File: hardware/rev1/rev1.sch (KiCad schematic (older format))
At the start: 28 parts, among them U1 BNO055, U2 MPL3115A2, U3 Teensy3.6, Y1 Crystal_32kHz768

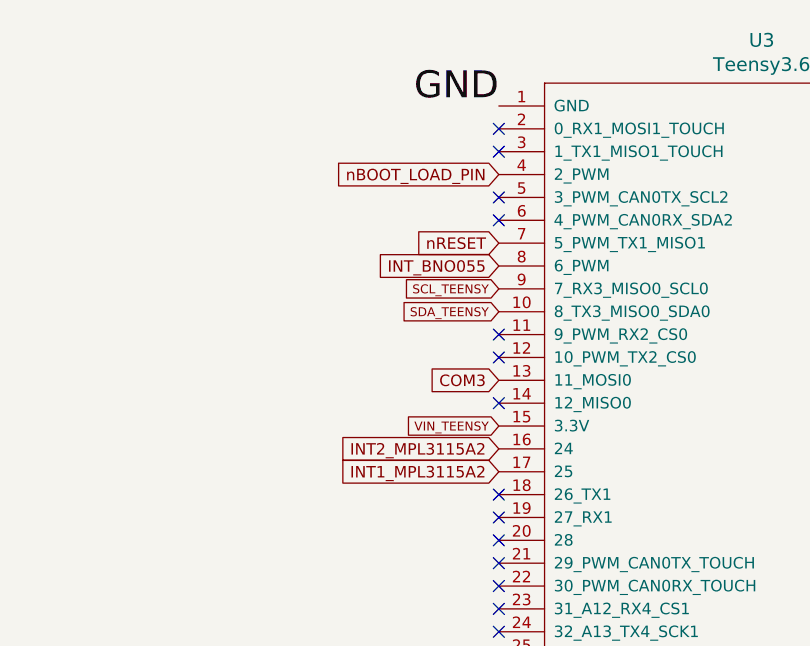
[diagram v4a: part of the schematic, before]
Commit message: mirror all components by flipping and manually reversing sides. Fixes BNO055 and MPL3115 footprint mirroring. (All other components also reversed but symmetrical. Teensy not flipped.) Reassign pins on Teensy.
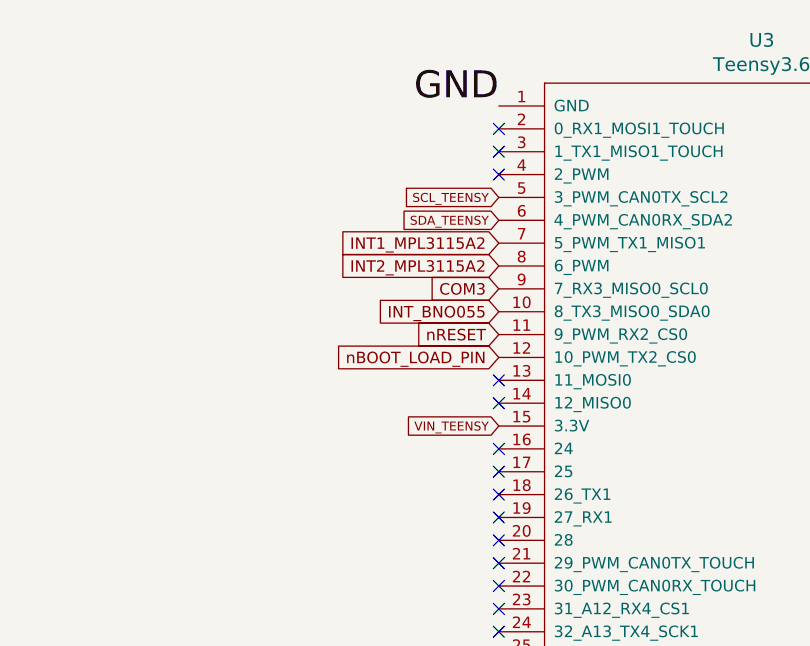
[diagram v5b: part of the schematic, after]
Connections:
- net COM3: now also U3.9 (7_RX3_MISO0_SCL0); no longer U3.13 (11_MOSI0)
- net INT1_MPL3115A2: now also U3.7 (5_PWM_TX1_MISO1); no longer U3.17 (25)
- net INT2_MPL3115A2: now also U3.8 (6_PWM); no longer U3.16 (24)
- net INT_BNO055: now also U3.10 (8_TX3_MISO0_SDA0); no longer U3.8 (6_PWM)
- net SCL_TEENSY: now also U3.5 (3_PWM_CAN0TX_SCL2); no longer U3.9 (7_RX3_MISO0_SCL0)
- net SDA_TEENSY: now also U3.6 (4_PWM_CAN0RX_SDA2); no longer U3.10 (8_TX3_MISO0_SDA0)
- net nBOOT_LOAD_PIN: now also U3.12 (10_PWM_TX2_CS0); no longer U3.4 (2_PWM)
- net nRESET: now also U3.11 (9_PWM_RX2_CS0); no longer U3.7 (5_PWM_TX1_MISO1)
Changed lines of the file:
@@
 Text Notes 26050 13750 0    50   ~ 0
 Vdd: power supply connection (1.95-3.6V)\nCAP: Ext. capacitor\nGND: Ground\nVddio: Digital interface power supply (1.62-3.6V)\nINT2: Pressure interrupt 2\nINT1: Pressure interrupt 1\nSDA: I2C serial data\nSDL: I2C serial clock
-$Comp
-L rev1-rescue:Teensy3.6-teensy U3
-U 1 1 60876FE4
-P 28550 4950
-F 0 "U3" H 28550 7387 60  0000 C CNN
-F 1 "Teensy3.6" H 28550 7281 60  0000 C CNN
-F 2 "footprints:Teensy3-6" H 28550 5000 60  0001 C CNN
-F 3 "" H 28550 5000 60  0000 C CNN
-	1    28550 4950
-	1    0    0    -1
-$EndComp
 Text Label 27400 2800 2    118  ~ 0
 GND
@@
 Text GLabel 9850 7300 2    50   Input ~ 0
 INT_BNO055
-Text GLabel 27400 4400 0    50   Input ~ 0
+Text GLabel 27400 3400 0    50   Input ~ 0
 INT1_MPL3115A2
-Text GLabel 27400 4300 0    50   Input ~ 0
+Text GLabel 27400 3500 0    50   Input ~ 0
 INT2_MPL3115A2
-Text GLabel 27400 3400 0    50   Input ~ 0
+Text GLabel 27400 3800 0    50   Input ~ 0
 nRESET
-Text GLabel 27400 3500 0    50   Input ~ 0
+Text GLabel 27400 3700 0    50   Input ~ 0
 INT_BNO055
-Text GLabel 27400 3100 0    50   Input ~ 0
+Text GLabel 27400 3900 0    50   Input ~ 0
 nBOOT_LOAD_PIN
-Text GLabel 27400 4000 0    50   Input ~ 0
+Text GLabel 27400 3600 0    50   Input ~ 0
 COM3
 Text GLabel 21600 2750 1    39   Input ~ 0
@@
 Wire Wire Line
 	11400 1800 10900 1800
-Text GLabel 27400 3600 0    39   Input ~ 0
+Text GLabel 27400 3200 0    39   Input ~ 0
 SCL_TEENSY
-Text GLabel 27400 3700 0    39   Input ~ 0
+Text GLabel 27400 3300 0    39   Input ~ 0
 SDA_TEENSY
 NoConn ~ 27400 2900
 NoConn ~ 27400 3000
-NoConn ~ 27400 3200
-NoConn ~ 27400 3300
-NoConn ~ 27400 3800
-NoConn ~ 27400 3900
 NoConn ~ 27400 4100
 NoConn ~ 27400 4500
@@
 NoConn ~ 27400 5700
 NoConn ~ 27400 5800
-NoConn ~ 27400 5900
-NoConn ~ 27400 6000
-NoConn ~ 27400 6100
-NoConn ~ 27400 6200
 NoConn ~ 27400 6300
 NoConn ~ 27400 6400
@@
 	28000 9300 28150 9300
 NoConn ~ 29700 6300
+NoConn ~ 27400 4300
+NoConn ~ 27400 4400
+NoConn ~ 27400 4000
+$Comp
+L rev1-rescue:Teensy3.6-teensy U3
+U 1 1 60876FE4
+P 28550 4950
+F 0 "U3" H 28550 7387 60  0000 C CNN
+F 1 "Teensy3.6" H 28550 7281 60  0000 C CNN
+F 2 "footprints:Teensy3-6" H 28550 5000 60  0001 C CNN
+F 3 "" H 28550 5000 60  0000 C CNN
+	1    28550 4950
+	1    0    0    -1
+$EndComp
+NoConn ~ 27400 3100
+NoConn ~ 27400 5900
+NoConn ~ 27400 6000
+NoConn ~ 27400 6100
+NoConn ~ 27400 6200
 $EndSCHEMATC

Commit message: add BMI088 and ADXL345 to schematic. Import ADXL345 from SnapEDA into separate schematic
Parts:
- added C10: C_0.1uF, footprints:C_0805_OEM, symbol preferred_parts:C_0.1uF
- added C11: C_1uF, footprints:C_0805_OEM, symbol preferred_parts:C_1uF
- added C12, C13: C_100nF, footprints:C_0603_1608Metric, symbol preferred_parts:C_100nF
- added J1, J2, J3: Conn_01x09_Male, symbol Connector:Conn_01x09_Male
- added U4: BMI088, footprints:bmi088, symbol preferred_parts:BMI088
- added U5: ADXL345BCCZ, ADXL345_snapEda:ADXL345, symbol ADXL345BCCZ:ADXL345BCCZ
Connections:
- net +3V3: now also C10.1, C11.1, C12.1, C13.1, J1.2 (Pin_2), J1.9 (Pin_9), U4.11 (VDDIO), U4.14 (CSB1), U4.3 (VDD), U4.7 (PS), U5.1 (VDD_I/O), U5.6 (VS), U5.7 (~CS)
- net GND: now also C10.2, C11.2, C12.2, C13.2, J1.3 (Pin_3), U4.4 (GNDA), U4.6 (GNDio), U5.12 (SDO/ALT_ADDRESS), U5.2 (GND), U5.4 (GND), U5.5 (GND)
- net SCL_TEENSY: now also U5.14 (SCL/SCLK)
- net SDA_TEENSY: now also U5.13 (SDA/SDI/SDIO)
- new net: U5.11 (RESERVED), U5.3 (RESERVED)
- new net ENABLE_GPS: J1.8 (Pin_8)
- new net FIX: J1.6 (Pin_6)
- new net INT1_ADXL345: U5.8 (INT1)
- new net INT2_ADXL345: U5.9 (INT2)
- new net PPS: J1.1 (Pin_1)
- new net RX: J1.4 (Pin_4)
- new net TX: J1.5 (Pin_5)
- new net V_BACKUP: J1.7 (Pin_7)
- no-connect marks 76 -> 79
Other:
- note added: "ADXL345"
- note added: "BMI088"
- note added: "GPS"
- note added: "POWER INPUT from BMS"
- note added: "Pull-up resistors exist on another part of the schematic."
- note added: "RADIO (Tentative, without connections yet)"
- note added: "These pull-up resistors (R3 and R4) should arguably be\nin a separate location on the schematic, as they affect\nthe entire I2C bus, not just the BNO055"
- note added: "VDDIO"
- note added: "ceramic capacitor preferred"
- note added: "tantalum capacitor preferred\nsee datasheet page 28."
- moved on the sheet: BMS_CONN1, BOOT1, C1, C2, C3, C4, C5, C6, CAP1, GND1, OSCin1, OSCout1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

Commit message: connect ADXL345 and BMI088 and GPS to Teensy in schematic
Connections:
- net V_BACKUP is gone; now on net +3V3: J1.7 (Pin_7)
- net A0_ACCEL_BMI088: now also U3.18 (26_TX1), U4.15 (SD01)
- net A0_GYRO_BMI088: now also U3.19 (27_RX1), U4.10 (SD02)
- net ENABLE_GPS: now also U3.32 (35_A16_PWM)
- net FIX: now also U3.35 (38_A19_PWM_SDA1)
- net INT1_ACCEL_BMI088: now also U3.24 (32_A13_TX4_SCK1), U4.16 (INT1)
- net INT1_ADXL345: now also U3.2 (0_RX1_MOSI1_TOUCH)
- net INT2_ACCEL_BMI088: now also U3.23 (31_A12_RX4_CS1), U4.1 (INT2)
- net INT2_ADXL345: now also U3.3 (1_TX1_MISO1_TOUCH)
- net INT3_GYRO_BMI088: now also U3.22 (30_PWM_CAN0RX_TOUCH), U4.12 (INT3)
- net INT4_GYRO_BMI088: now also U3.21 (29_PWM_CAN0TX_TOUCH), U4.13 (INT4)
- net PPS: now also U3.33 (36_A17_PWM)
- net RX: now also U3.31 (34_A15_CAN1TX_SDA0)
- net SCL_TEENSY: now also U4.8 (SCx)
- net SDA_TEENSY: now also U4.9 (SDx)
- net TX: now also U3.30 (33_A14_CAN1TX_SCL0)
- no-connect marks 79 -> 84
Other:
- moved on the sheet: C12, C13

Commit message: wip
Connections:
- net A0_ACCEL_BMI088: now also U3.19 (27_RX1); no longer U3.18 (26_TX1)
- net A0_GYRO_BMI088: now also U3.18 (26_TX1); no longer U3.19 (27_RX1)
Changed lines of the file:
@@
 Text GLabel 27400 4800 0    50   Input ~ 0
 INT4_GYRO_BMI088
+Text GLabel 27400 4500 0    50   Input ~ 0
+A0_GYRO_BMI088
 Text GLabel 27400 4600 0    50   Input ~ 0
-A0_GYRO_BMI088
-Text GLabel 27400 4500 0    50   Input ~ 0
 A0_ACCEL_BMI088
 Text GLabel 27400 5800 0    50   Input ~ 0
